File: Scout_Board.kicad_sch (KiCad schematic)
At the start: 31 parts

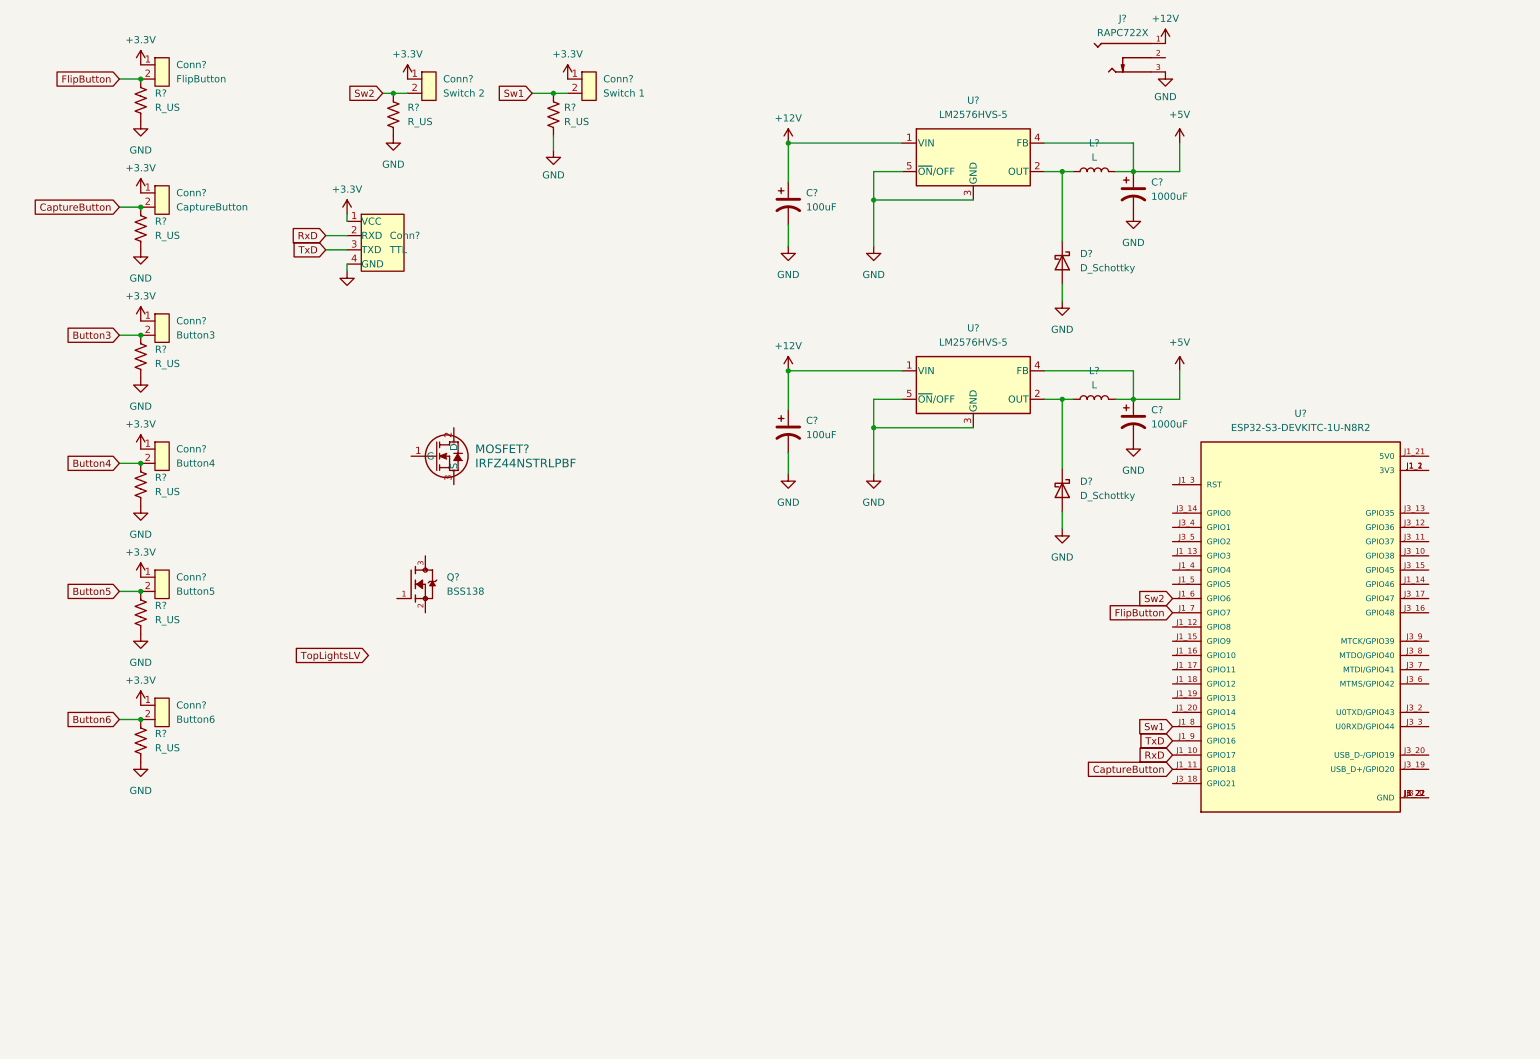
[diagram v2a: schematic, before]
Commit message: Circuit done except motor
Need to add smd buttons.
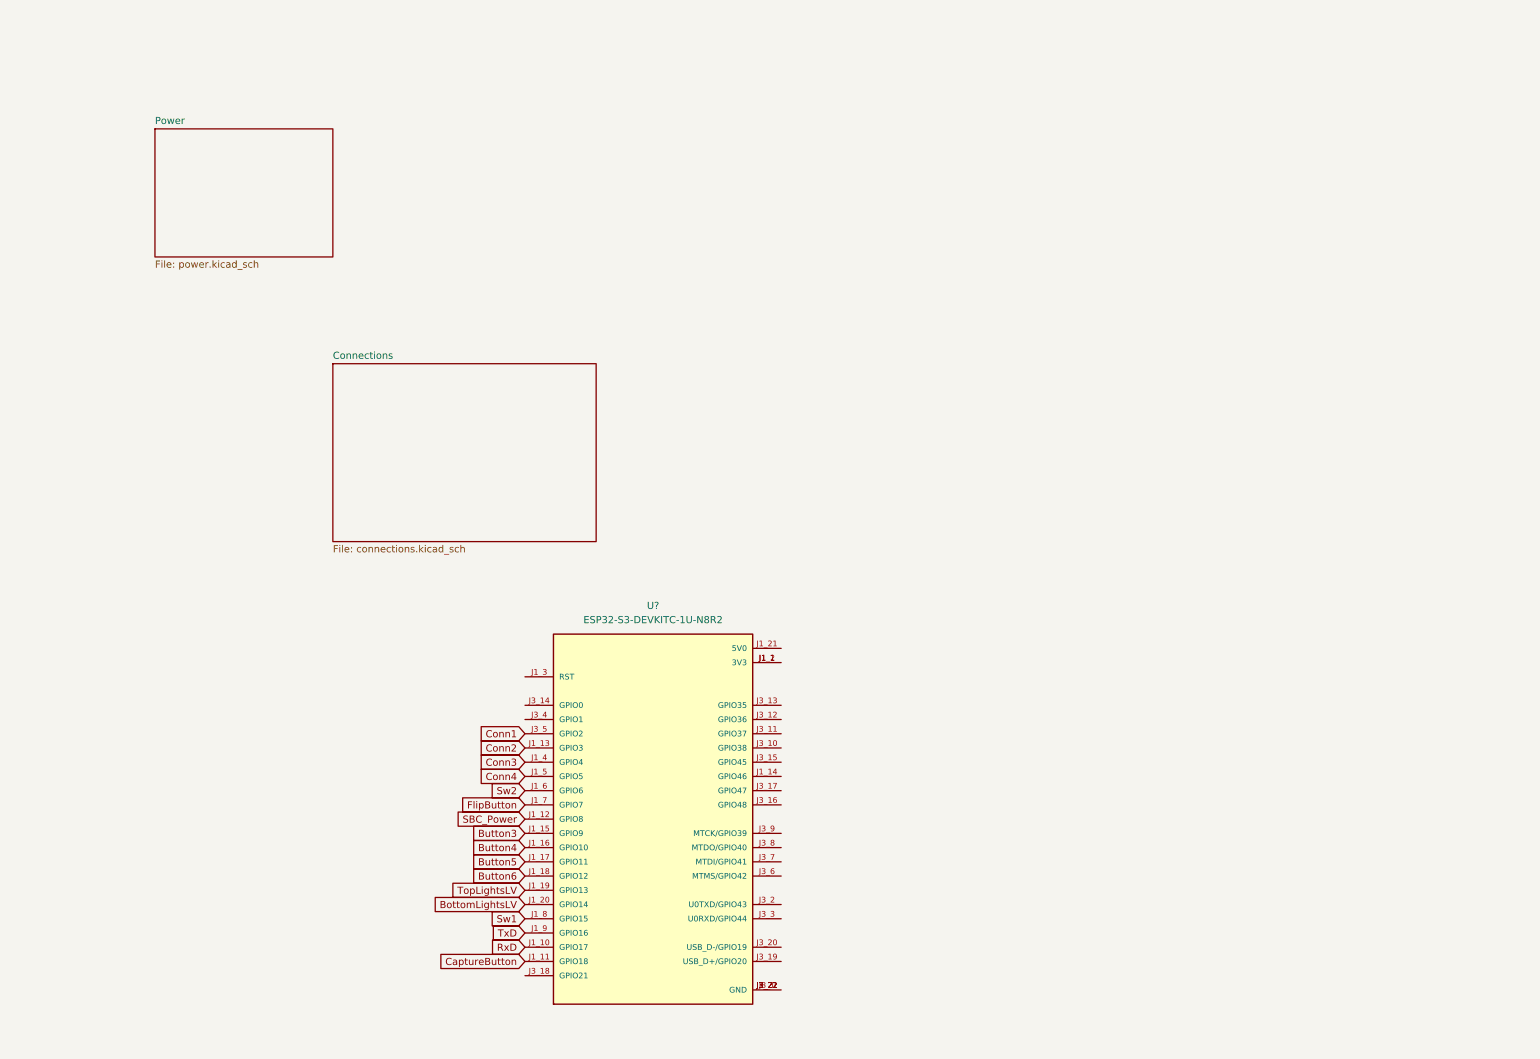
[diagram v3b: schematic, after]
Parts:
- removed C? (x2): 100uF, symbol Device:C_Polarized_US
- removed C? (x2): 1000uF, symbol Device:C_Polarized_US
- removed Conn?: Button3, symbol Scout_library:B2B_VERT_1.5MM
- removed Conn?: Switch 2, symbol Scout_library:B2B_VERT_1.5MM
- removed Conn?: Button4, symbol Scout_library:B2B_VERT_1.5MM
- removed Conn?: FlipButton, symbol Scout_library:B2B_VERT_1.5MM
- removed Conn?: CaptureButton, symbol Scout_library:B2B_VERT_1.5MM
- removed Conn?: Switch 1, symbol Scout_library:B2B_VERT_1.5MM
- removed Conn?: TTL, symbol Scout_library:B4B_VERT_1.5MM
- removed Conn?: Button6, symbol Scout_library:B2B_VERT_1.5MM
- removed Conn?: Button5, symbol Scout_library:B2B_VERT_1.5MM
- removed D? (x2): D_Schottky, symbol Device:D_Schottky
- removed J?: RAPC722X, RAPC722X:SWITCHCRAFT_RAPC722X, symbol RAPC722X:RAPC722X
- removed L? (x2): L, symbol Device:L
- removed MOSFET?: IRFZ44NSTRLPBF, Downloaded_footprints:D2PAK_INF, symbol 2024-05-21_14-07-33:IRFZ44NSTRLPBF
- removed Q?: BSS138, BSS138:SOT95P240X111-3N, symbol BSS138:BSS138
- removed R? (x8): R_US, symbol Device:R_US
- removed U? (x2): LM2576HVS-5, Package_TO_SOT_SMD:TO-263-5_TabPin3, symbol Regulator_Switching:LM2576HVS-5
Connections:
- net Button3: now also U?.J1_15 (GPIO9)
- net Button4: now also U?.J1_16 (GPIO10)
- net Button5: now also U?.J1_17 (GPIO11)
- net Button6: now also U?.J1_18 (GPIO12)
- net TopLightsLV: now also U?.J1_19 (GPIO13)
- net SBC_Power: now reaches U?.J1_12 (GPIO8)
- net Conn2: now reaches U?.J1_13 (GPIO3)
- net BottomLightsLV: now reaches U?.J1_20 (GPIO14)
- net Conn3: now reaches U?.J1_4 (GPIO4)
- net Conn4: now reaches U?.J1_5 (GPIO5)
- net Conn1: now reaches U?.J3_5 (GPIO2)
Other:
- added sheet Connections (connections.kicad_sch)
- added sheet Power (power.kicad_sch)
- moved on the sheet: U?

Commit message: Finished circuit
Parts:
- added C1: 0.1uF/50V, symbol Device:C_Small
- added C2: 22uF/63V, symbol Device:C_Polarized_Small
- added R1: 30k, symbol Device:R_Small_US
- added U1: DRV8871DDA, Package_SO:Texas_HTSOP-8-1EP_3.9x4.9mm_P1.27mm_EP2.95x4.9mm_Mask2.4x3.1mm_ThermalVias, symbol dk_PMIC-Motor-Drivers-Controllers:DRV8871DDA
- gave numbers to parts that had none: 1
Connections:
- net +3.3V: now reaches U2.J1_1 (3V3), U2.J1_2 (3V3)
- net +5V: now reaches U2.J1_21 (5V0)
- net GND: now reaches U2.J1_22 (GND), U2.J3_1 (GND), U2.J3_21 (GND), U2.J3_22 (GND)
- net GND: now also C1.2, C2.2, R1.2, U1.1 (GND), U1.7 (PGND), U1.9
- net IN2: now reaches U2.J3_13 (GPIO35)
- net IN2: now also U1.2 (IN2)
- net IN1: now reaches U2.J3_18 (GPIO21)
- net IN1: now also U1.3 (IN1)
- new net: R1.1, U1.4 (ILIM)
- new net +12V: C1.1, C2.1, U1.5 (VM)
- new net OUT1: U1.6 (OUT1)
- new net OUT2: U1.8 (OUT2)
- no-connect marks 0 -> 18

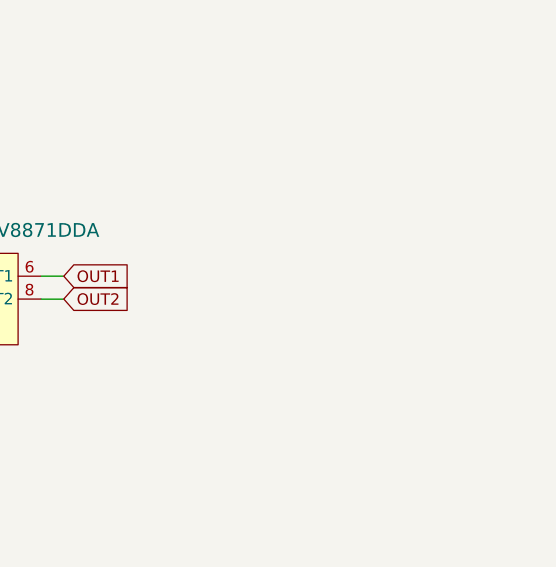
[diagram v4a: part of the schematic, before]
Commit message: Updated the footprints for all the components.
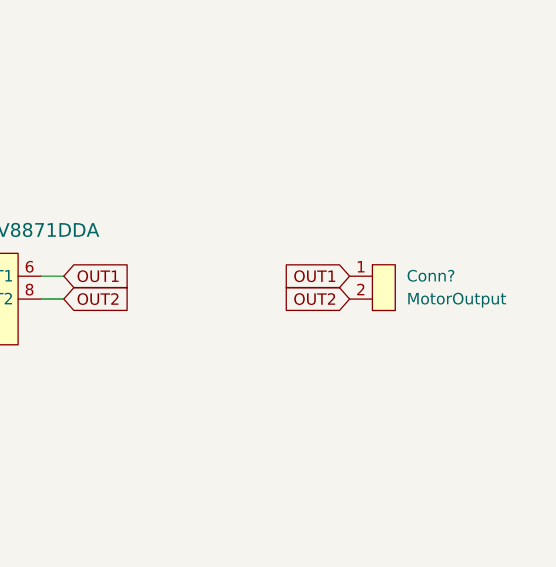
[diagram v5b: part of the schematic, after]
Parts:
- added Conn?: MotorOutput, Downloaded_footprints:CONN_B2B-ZRLFSN_JST, symbol Scout_library:B2B_VERT_1.5MM
- C1: footprint (none) -> Capacitor_SMD:C_0603_1608Metric_Pad1.08x0.95mm_HandSolder
- C2: footprint (none) -> EEH_ZA1J220XP:CAP_EEHZA1J220XP
- R1: footprint (none) -> Resistor_SMD:R_0603_1608Metric_Pad0.98x0.95mm_HandSolder
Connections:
- net OUT1: now also Conn?.1 (Pin_1)
- net OUT2: now also Conn?.2 (Pin_2)
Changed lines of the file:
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@@
+    )
+  )
+  (global_label "OUT2" (shape input) (at 243.84 64.77 180) (fields_autoplaced)
+    (effects (font (size 1.27 1.27)) (justify right))
+    (property "Intersheetrefs" "${INTERSHEET_REFS}" (at 236.0167 64.77 0)
+      (effects (font (size 1.27 1.27)) (justify right) hide)
     )
   )
@@
     )
   )
+  (global_label "OUT1" (shape input) (at 243.84 62.23 180) (fields_autoplaced)
+    (effects (font (size 1.27 1.27)) (justify right))
+    (property "Intersheetrefs" "${INTERSHEET_REFS}" (at 236.0167 62.23 0)
+      (effects (font (size 1.27 1.27)) (justify right) hide)
+    )
+  )
   (global_label "Conn1" (shape input) (at 97.79 139.7 180) (fields_autoplaced)
     (effects (font (size 1.27 1.27)) (justify right))
@@
     (property "Intersheetrefs" "${INTERSHEET_REFS}" (at 91.2367 177.8 0)
       (effects (font (size 1.27 1.27)) (justify right) hide)
+    )
+  )
+  (symbol (lib_id "Scout_library:B2B_VERT_1.5MM") (at 247.65 59.69 0) (unit 1)
+    (in_bom yes) (on_board yes) (dnp no) (fields_autoplaced)
+    (property "Reference" "Conn?" (at 250.19 62.23 0)
+      (effects (font (size 1.27 1.27)) (justify left))
+    )
+    (property "Value" "MotorOutput" (at 250.19 64.77 0)
+      (effects (font (size 1.27 1.27)) (justify left))
+    )
+    (property "Footprint" "Downloaded_footprints:CONN_B2B-ZRLFSN_JST" (at 247.65 59.69 0)
+      (effects (font (size 1.27 1.27)) hide)
+    )
+    (property "Datasheet" "https://www.jst-mfg.com/product/pdf/eng/eZH.pdf" (at 247.65 59.69 0)
+      (effects (font (size 1.27 1.27)) hide)
+    )
+    (pin "2")
+    (pin "1")
+    (instances
+      (project "Scout_Board"
+        (path "/e58a9779-147f-4c0c-a745-6e9bc8ec0357"
+          (reference "Conn?") (unit 1)
+        )
+      )
     )
   )
@@
       (effects (font (size 1.27 1.27)) (justify left))
     )
-    (property "Footprint" "" (at 193.04 49.53 0)
+    (property "Footprint" "EEH_ZA1J220XP:CAP_EEHZA1J220XP" (at 193.04 49.53 0)
       (effects (font (size 1.27 1.27)) hide)
     )
@@
       (effects (font (size 1.27 1.27)) (justify left))
     )
-    (property "Footprint" "" (at 180.34 49.53 0)
+    (property "Footprint" "Capacitor_SMD:C_0603_1608Metric_Pad1.08x0.95mm_HandSolder" (at 180.34 49.53 0)
       (effects (font (size 1.27 1.27)) hide)
     )
@@
       (effects (font (size 1.27 1.27)) (justify left))
     )
-    (property "Footprint" "" (at 184.15 72.39 0)
-      (effects (font (size 1.27 1.27)) hide)
-    )
+    (property "Footprint" "Resistor_SMD:R_0603_1608Metric_Pad0.98x0.95mm_HandSolder" (at 184.15 72.39 0)
+      (effects (font (size 1.27 1.27)) hide)
+    )

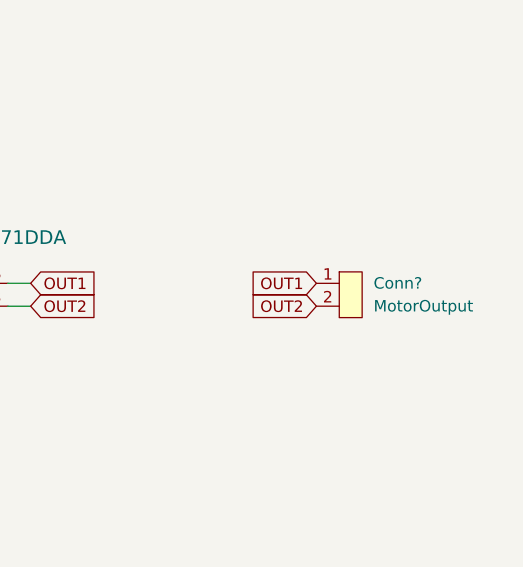
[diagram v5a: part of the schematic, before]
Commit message: PCB Layout done
Routing yet to do.
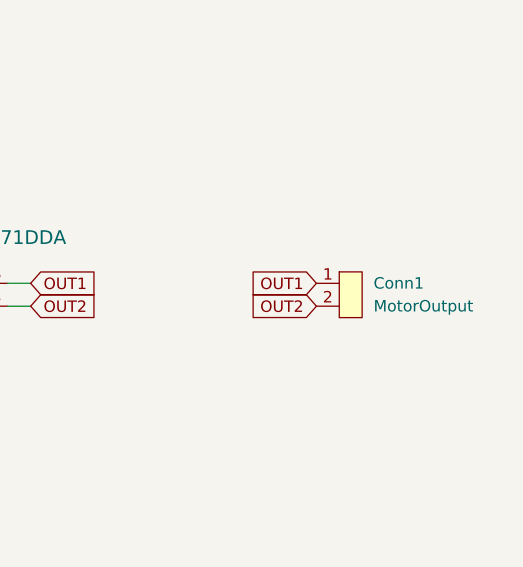
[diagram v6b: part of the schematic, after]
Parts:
- U2: footprint ESP32-S3-DEVKITC-1U-N8R2:XCVR_ESP32-S3-DEVKITC-1U-N8R2 -> Downloaded_footprints:XCVR_ESP32-S3-DEVKITC-1U-N8R2
- gave numbers to parts that had none: 1
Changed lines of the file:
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@@
   (symbol (lib_id "Scout_library:B2B_VERT_1.5MM") (at 247.65 59.69 0) (unit 1)
     (in_bom yes) (on_board yes) (dnp no) (fields_autoplaced)
-    (property "Reference" "Conn?" (at 250.19 62.23 0)
+    (property "Reference" "Conn1" (at 250.19 62.23 0)
       (effects (font (size 1.27 1.27)) (justify left))
     )
@@
       (project "Scout_Board"
         (path "/e58a9779-147f-4c0c-a745-6e9bc8ec0357"
-          (reference "Conn?") (unit 1)
+          (reference "Conn1") (unit 1)
         )
       )
@@
       (effects (font (size 1.27 1.27)))
     )
-    (property "Footprint" "ESP32-S3-DEVKITC-1U-N8R2:XCVR_ESP32-S3-DEVKITC-1U-N8R2" (at 120.65 154.94 0)
+    (property "Footprint" "Downloaded_footprints:XCVR_ESP32-S3-DEVKITC-1U-N8R2" (at 120.65 154.94 0)
       (effects (font (size 1.27 1.27)) (justify bottom) hide)
     )
